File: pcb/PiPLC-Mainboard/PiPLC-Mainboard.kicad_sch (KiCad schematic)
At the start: 142 parts, among them J1 WJ2EDGRC-5.08-4P, J10 WJ2EDGRC-5.08-4P, J11 WJ2EDGRC-5.08-4P, J12 WJ2EDGRC-5.08-4P, J13 Modbus, J17 Conn_02x12_Odd_Even, J3 WJ2EDGRC-5.08-4P, J4 WJ2EDGRC-5.08-4P, J5 WJ2EDGRC-5.08-4P, J6 WJ2EDGRC-5.08-4P, J7 WJ2EDGRC-5.08-4P, J8 WJ2EDGRC-5.08-4P, J9 WJ2EDGRC-5.08-4P, J99 Rpi GPIO, K1 G5RL-1A-E-TV8 DC24, K2 G5RL-1A-E-TV8 DC24, K3 G5RL-1A-E-TV8 DC24, K4 G5RL-1A-E-TV8 DC24, K5 G5RL-1A-E-TV8 DC24, K6 G5RL-1A-E-TV8 DC24, K7 G5RL-1A-E-TV8 DC24, K8 G5RL-1A-E-TV8 DC24, Q1 AO3400A, Q2 AO3400A, Q3 AO3400A, Q4 AO3400A, Q5 AO3400A, Q6 AO3400A, Q7 AO3400A, Q8 AO3400A, U1 TPS54331D, U10 EL817C, U11 EL817C, U12 ISO3082DWR, U2 NCN5121, U3 ISO1540, U4 EL817C, U5 EL817C, U6 EL817C, U7 EL817C, U8 EL817C, U9 EL817C, Y2 16MHz

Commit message: Rename both PCBs and align their connector
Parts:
- J17: footprint Connector_PinHeader_2.54mm:PinHeader_2x12_P2.54mm_Vertical -> Connector_PinSocket_2.54mm:PinSocket_2x12_P2.54mm_Vertical

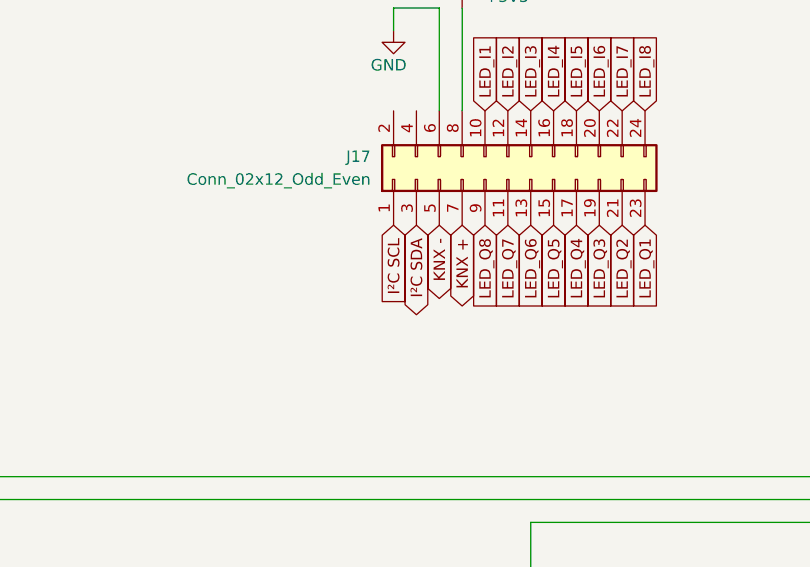
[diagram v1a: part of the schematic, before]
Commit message: [Mainboard][HMI] Remove display
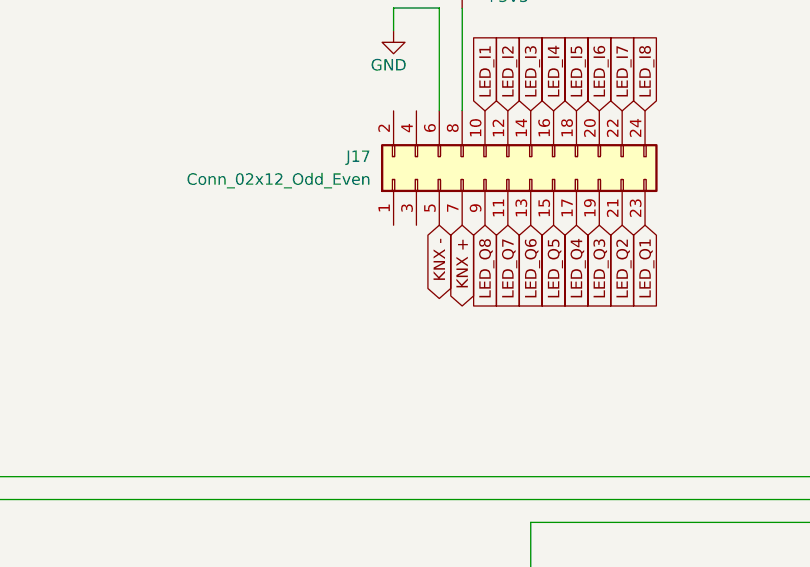
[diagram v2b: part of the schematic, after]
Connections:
- net I²C SCL renamed GPIO_03
- net GPIO_03: no longer J17.1 (Pin_1)
- net I²C SDA renamed GPIO_02
- net GPIO_02: no longer J17.3 (Pin_3)
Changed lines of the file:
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@@
-    )
-  )
-  (global_label "I²C SCL" (shape input) (at 180.34 246.38 270) (fields_autoplaced)
-    (effects (font (size 1.27 1.27)) (justify right))
-    (property "Intersheetrefs" "${INTERSHEET_REFS}" (at 180.34 256.6828 90)
-      (effects (font (size 1.27 1.27)) (justify right) hide)
     )
   )
@@
       (effects (font (size 1.27 1.27)) (justify right) hide)
     )
-  )
-  (global_label "I²C SDA" (shape bidirectional) (at 182.88 246.38 270) (fields_autoplaced)
-    (effects (font (size 1.27 1.27)) (justify right))
-    (property "Intersheetrefs" "${INTERSHEET_REFS}" (at 182.88 257.8546 90)
-      (effects (font (size 1.27 1.27)) (justify right) hide)
-    )

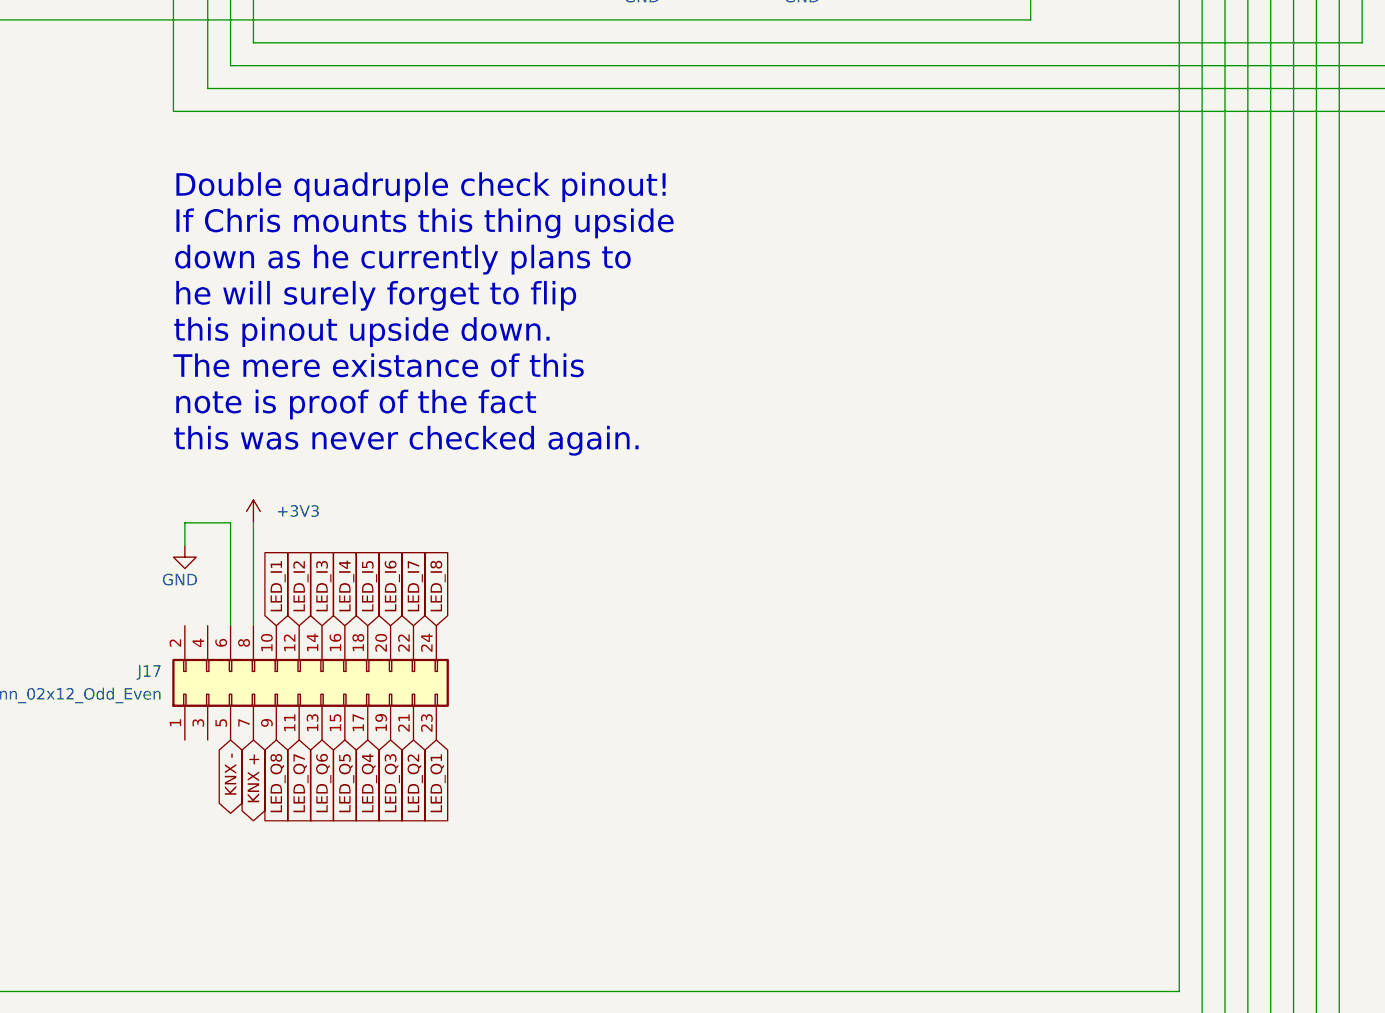
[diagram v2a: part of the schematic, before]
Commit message: Add "5V OK" and "24V OK" LEDs to HMI
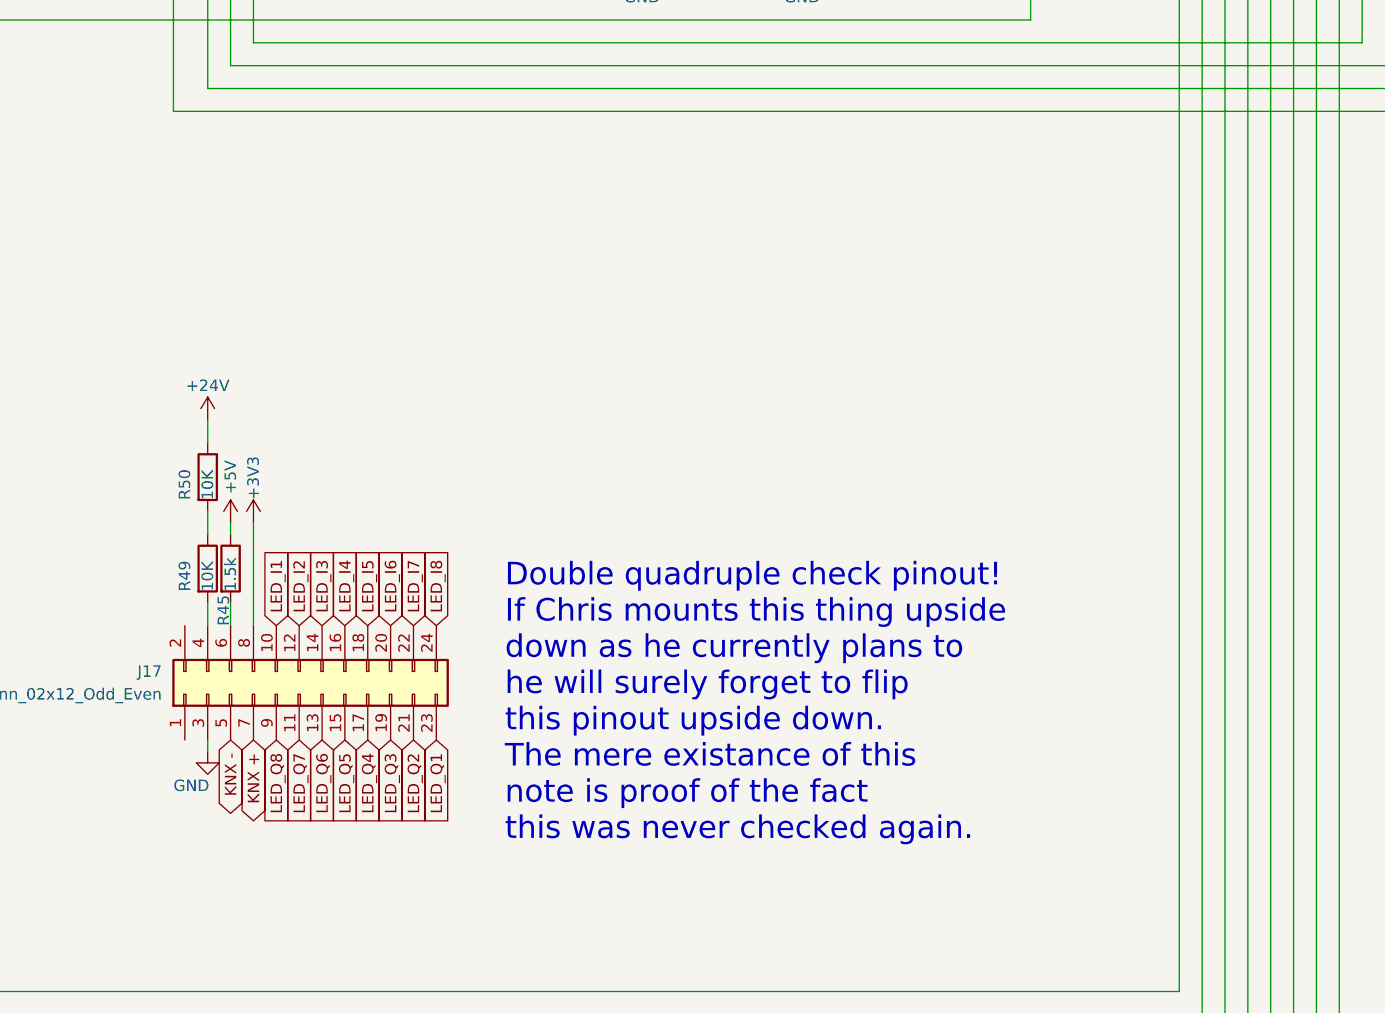
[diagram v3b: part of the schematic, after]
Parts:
- added R45: 1.5k, Resistor_SMD:R_0603_1608Metric, symbol Device:R
- added R49, R50: 10K, Resistor_SMD:R_0603_1608Metric, symbol Device:R
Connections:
- net +24V: now also R50.1
- net +5V: now also R45.1
- net GND: now also J17.3 (Pin_3); no longer J17.6 (Pin_6)
- net at J17.4 (Pin_4): now also R49.2
- new net: R49.1, R50.2
- new net: J17.6 (Pin_6), R45.2
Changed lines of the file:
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@@
     (stroke (width 0) (type default))
   )
+  (wire (pts (xy 182.88 210.82) (xy 182.88 213.36))
+    (stroke (width 0) (type default))
+  )
   (wire (pts (xy 276.86 313.69) (xy 276.86 314.96))
     (stroke (width 0) (type default))
@@
     (stroke (width 0) (type default))
   )
-  (wire (pts (xy 180.34 222.25) (xy 185.42 222.25))
-    (stroke (width 0) (type default))
-  )
   (polyline (pts (xy 140.97 360.68) (xy 140.97 354.33))
     (stroke (width 0) (type solid))
@@
     (stroke (width 0) (type default))
   )
-  (wire (pts (xy 180.34 224.79) (xy 180.34 222.25))
+  (wire (pts (xy 182.88 247.65) (xy 182.88 246.38))
     (stroke (width 0) (type default))
   )
@@
     (stroke (width 0) (type default))
   )
+  (wire (pts (xy 185.42 222.25) (xy 185.42 223.52))
+    (stroke (width 0) (type default))
+  )
   (wire (pts (xy 379.73 78.74) (xy 379.73 76.2))
     (stroke (width 0) (type default))
@@
     (stroke (width 0) (type default))
   )
+  (wire (pts (xy 185.42 231.14) (xy 185.42 233.68))
+    (stroke (width 0) (type default))
+  )
   (wire (pts (xy 533.4 316.23) (xy 533.4 345.44))
     (stroke (width 0) (type default))
@@
     (stroke (width 0) (type default))
   )
+  (wire (pts (xy 182.88 231.14) (xy 182.88 233.68))
+    (stroke (width 0) (type default))
+  )
   (wire (pts (xy 398.78 326.39) (xy 398.78 331.47))
     (stroke (width 0) (type default))
@@
     (stroke (width 0) (type default))
   )
-  (wire (pts (xy 185.42 222.25) (xy 185.42 233.68))
-    (stroke (width 0) (type default))
-  )
   (wire (pts (xy 403.86 193.04) (xy 406.4 193.04))
     (stroke (width 0) (type default))
@@
     (stroke (width 0) (type default))
   )
+  (wire (pts (xy 182.88 220.98) (xy 182.88 223.52))
+    (stroke (width 0) (type default))
+  )
   (wire (pts (xy 198.12 97.79) (xy 198.12 71.12))
     (stroke (width 0) (type default))
@@
   )
   (text "Double quadruple check pinout!\nIf Chris mounts this thing upside\ndown as he currently plans to\nhe will surely forget to flip\nthis pinout upside down.\nThe mere existance of this\nnote is proof of the fact\nthis was never checked again."
-    (at 179.07 214.63 0)
+    (at 215.9 257.81 0)
     (effects (font (size 2.5 2.5)) (justify left bottom))
   )
@@
     )
   )
+  (symbol (lib_id "Device:R") (at 182.88 217.17 0) (unit 1)
+    (in_bom yes) (on_board yes) (dnp no)
+    (property "Reference" "R50" (at 180.34 219.71 90)
+      (effects (font (size 1.27 1.27)) (justify left))
+    )
+    (property "Value" "10K" (at 182.88 219.71 90)
+      (effects (font (size 1.27 1.27)) (justify left))
+    )
+    (property "Footprint" "Resistor_SMD:R_0603_1608Metric" (at 181.102 217.17 90)
+      (effects (font (size 1.27 1.27)) hide)
+    )
+    (property "Datasheet" "~" (at 182.88 217.17 0)
+      (effects (font (size 1.27 1.27)) hide)
+    )
+    (property "LCSC" "C25804" (at 182.88 217.17 0)
+      (effects (font (size 1.27 1.27)) hide)
+    )
+    (pin "1")
+    (pin "2")
+    (instances
+      (project "PiPLC-Mainboard"
+        (path "/93ebf745-625a-4d9e-8f47-45e91f30ef94"
+          (reference "R50") (unit 1)
+        )
+      )
+      (project "ESP-Hiro"
+        (path "/abafd663-d05f-485e-8552-fce51763e477"
+          (reference "R14") (unit 1)
+        )
+      )
+    )
+  )
   (symbol (lib_id "power:GND") (at 95.25 251.46 0) (unit 1)
     (in_bom yes) (on_board yes) (dnp no)
@@
     )
   )
+  (symbol (lib_id "power:+24V") (at 182.88 210.82 0) (unit 1)
+    (in_bom yes) (on_board yes) (dnp no)
+    (property "Reference" "#PWR083" (at 182.88 214.63 0)
+      (effects (font (size 1.27 1.27)) hide)
+    )
+    (property "Value" "+24V" (at 182.88 207.01 0)
+      (effects (font (size 1.27 1.27)))
+    )
+    (property "Footprint" "" (at 182.88 210.82 0)
+      (effects (font (size 1.27 1.27)) hide)
+    )
+    (property "Datasheet" "" (at 182.88 210.82 0)
+      (effects (font (size 1.27 1.27)) hide)
+    )
+    (pin "1")
+    (instances
+      (project "PiPLC-Mainboard"
+        (path "/93ebf745-625a-4d9e-8f47-45e91f30ef94"
+          (reference "#PWR083") (unit 1)
+        )
+      )
+    )
+  )
   (symbol (lib_id "power:+24V") (at 243.84 26.67 0) (unit 1)
     (in_bom yes) (on_board yes) (dnp no) (fields_autoplaced)
@@
   )
   (symbol (lib_id "power:+3V3") (at 187.96 222.25 0) (unit 1)
-    (in_bom yes) (on_board yes) (dnp no) (fields_autoplaced)
+    (in_bom yes) (on_board yes) (dnp no)
     (property "Reference" "#PWR046" (at 187.96 226.06 0)
       (effects (font (size 1.27 1.27)) hide)
     )
-    (property "Value" "+3V3" (at 190.5 220.98 0)
+    (property "Value" "+3V3" (at 187.96 219.71 90)
       (effects (font (size 1.27 1.27)) (justify left))
     )
@@
     )
   )
+  (symbol (lib_id "Device:R") (at 185.42 227.33 0) (unit 1)
+    (in_bom yes) (on_board yes) (dnp no)
+    (property "Reference" "R45" (at 184.6512 233.6873 90)
+      (effects (font (size 1.27 1.27)) (justify left))
+    )
+    (property "Value" "1.5k" (at 185.42 229.87 90)
+      (effects (font (size 1.27 1.27)) (justify left))
+    )
+    (property "Footprint" "Resistor_SMD:R_0603_1608Metric" (at 183.642 227.33 90)
+      (effects (font (size 1.27 1.27)) hide)
+    )
+    (property "Datasheet" "~" (at 185.42 227.33 0)
+      (effects (font (size 1.27 1.27)) hide)
+    )
+    (property "LCSC" "C22843" (at 185.42 227.33 0)
+      (effects (font (size 1.27 1.27)) hide)
+    )
+    (pin "1")
+    (pin "2")
+    (instances
+      (project "PiPLC-Mainboard"
+        (path "/93ebf745-625a-4d9e-8f47-45e91f30ef94"
+          (reference "R45") (unit 1)
+        )
+      )
+      (project "ESP-Hiro"
+        (path "/abafd663-d05f-485e-8552-fce51763e477"
+          (reference "R15") (unit 1)
+        )
+      )
+    )
+  )
   (symbol (lib_id "Device:C") (at 100.33 236.22 0) (unit 1)
     (in_bom yes) (on_board yes) (dnp no)
@@
     )
   )
-  (symbol (lib_id "power:GND") (at 180.34 224.79 0) (unit 1)
+  (symbol (lib_id "power:GND") (at 182.88 247.65 0) (unit 1)
     (in_bom yes) (on_board yes) (dnp no)
-    (property "Reference" "#PWR045" (at 180.34 231.14 0)
+    (property "Reference" "#PWR045" (at 182.88 254 0)
       (effects (font (size 1.27 1.27)) hide)
     )
-    (property "Value" "GND" (at 177.8 228.6 0)
+    (property "Value" "GND" (at 179.07 251.46 0)
       (effects (font (size 1.27 1.27)) (justify left))
     )
-    (property "Footprint" "" (at 180.34 224.79 0)
+    (property "Footprint" "" (at 182.88 247.65 0)
       (effects (font (size 1.27 1.27)) hide)
     )
-    (property "Datasheet" "" (at 180.34 224.79 0)
+    (property "Datasheet" "" (at 182.88 247.65 0)
       (effects (font (size 1.27 1.27)) hide)
     )
@@
     )
   )
+  (symbol (lib_id "power:+5V") (at 185.42 222.25 0) (unit 1)
+    (in_bom yes) (on_board yes) (dnp no)
+    (property "Reference" "#PWR079" (at 185.42 226.06 0)
+      (effects (font (size 1.27 1.27)) hide)
+    )
+    (property "Value" "+5V" (at 185.42 217.17 90)
+      (effects (font (size 1.27 1.27)))
+    )
+    (property "Footprint" "" (at 185.42 222.25 0)
+      (effects (font (size 1.27 1.27)) hide)
+    )
+    (property "Datasheet" "" (at 185.42 222.25 0)
+      (effects (font (size 1.27 1.27)) hide)
+    )
+    (pin "1")
+    (instances
+      (project "PiPLC-Mainboard"
+        (path "/93ebf745-625a-4d9e-8f47-45e91f30ef94"
+          (reference "#PWR079") (unit 1)
+        )
+      )
+      (project "ESP-Hiro"
+        (path "/abafd663-d05f-485e-8552-fce51763e477"
+          (reference "#PWR021") (unit 1)
+        )
+      )
+    )
+  )
   (symbol (lib_id "power:GND") (at 54.61 77.47 0) (unit 1)
     (in_bom yes) (on_board yes) (dnp no)
@@
         )
       )
+    )
+  )
+  (symbol (lib_id "Device:R") (at 182.88 227.33 0) (unit 1)
+    (in_bom yes) (on_board yes) (dnp no)
+    (property "Reference" "R49" (at 180.34 229.87 90)
+      (effects (font (size 1.27 1.27)) (justify left))
+    )
+    (property "Value" "10K" (at 182.88 229.87 90)
+      (effects (font (size 1.27 1.27)) (justify left))
+    )
+    (property "Footprint" "Resistor_SMD:R_0603_1608Metric" (at 181.102 227.33 90)
+      (effects (font (size 1.27 1.27)) hide)
+    )
+    (property "Datasheet" "~" (at 182.88 227.33 0)
+      (effects (font (size 1.27 1.27)) hide)
+    )
+    (property "LCSC" "C25804" (at 182.88 227.33 0)
+      (effects (font (size 1.27 1.27)) hide)
+    )
+    (pin "1")
+    (pin "2")
+    (instances
+      (project "PiPLC-Mainboard"
+        (path "/93ebf745-625a-4d9e-8f47-45e91f30ef94"
+          (reference "R49") (unit 1)
+        )
+      )
+      (project "ESP-Hiro"
+        (path "/abafd663-d05f-485e-8552-fce51763e477"
+          (reference "R14") (unit 1)
+        )
+      )

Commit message: [Main] Run ERC
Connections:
- net GND: now also J1.3 (Pin_3), J1.4 (Pin_4)
- net GPIO_02 renamed I²C SDA
- net GPIO_03 renamed I²C SCL
- net GPIO_04 renamed UART3_RpiTX
- net GPIO_05 renamed UART3_RpiRX
- net GPIO_06 renamed UART3_RpiRTS
- net GPIO_07 renamed Q4
- net GPIO_08 renamed Q3
- net GPIO_09 renamed I5
- net GPIO_10 renamed I4
- net GPIO_11 renamed I6
- net GPIO_12 renamed Q5
- net GPIO_13 renamed I7
- net GPIO_14 renamed UART0_RpiTX
- net GPIO_15 renamed UART0_RpiRX
- net GPIO_16 renamed Q6
- net GPIO_17 renamed I1
- net GPIO_18 renamed PWM_0
- net GPIO_19 renamed PWM_1
- net GPIO_20 renamed Q7
- net GPIO_21 renamed Q8
- net GPIO_22 renamed I3
- net GPIO_24 renamed Q1
- net GPIO_25 renamed Q2
- net GPIO_26 renamed I8
- net GPIO_27 renamed I2
- no-connect marks 64 -> 66
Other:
- note added: "GPIO_02"
- note added: "GPIO_03"
- note added: "GPIO_04"
- note added: "GPIO_05"
- note added: "GPIO_06"
- note added: "GPIO_07"
- note added: "GPIO_08"
- note added: "GPIO_09"
- note added: "GPIO_10"
- note added: "GPIO_11"
- note added: "GPIO_12"
- note added: "GPIO_13"
- note added: "GPIO_14"
- note added: "GPIO_15"
- note added: "GPIO_16"
- note added: "GPIO_17"
- note added: "GPIO_18"
- note added: "GPIO_19"
- note added: "GPIO_20"
- note added: "GPIO_21"
- note added: "GPIO_22"
- note added: "GPIO_23"
- note added: "GPIO_24"
- note added: "GPIO_25"
- note added: "GPIO_26"
- note added: "GPIO_27"
- note removed: "OpenPLC %IX0.3"
- note removed: "OpenPLC %IX0.4"
- note removed: "OpenPLC %IX0.5"
- note removed: "OpenPLC %IX0.6"
- note removed: "OpenPLC %IX0.7"
- note removed: "OpenPLC %IX1.0"
- note removed: "OpenPLC %IX1.3"
- note removed: "OpenPLC %IX1.4"
- note removed: "OpenPLC %IX1.5"
- note removed: "OpenPLC %QX0.2"
- note removed: "OpenPLC %QX0.3"
- note removed: "OpenPLC %QX0.4"
- note removed: "OpenPLC %QX0.5"
- note removed: "OpenPLC %QX0.6"
- note removed: "OpenPLC %QX0.7"
- note removed: "OpenPLC %QX1.0"
- note removed: "OpenPLC %QX1.1"
- note removed: "OpenPLC %QX1.2"

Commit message: [Main][HMI]Minor schematic beautification
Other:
- moved on the sheet: C18
